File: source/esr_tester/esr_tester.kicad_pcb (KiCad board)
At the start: 2 copper layers, 48.3 x 71.1 mm, 40 parts, among them IC1-1 TL084, J1 Conn_01x01, J2 Conn_01x01

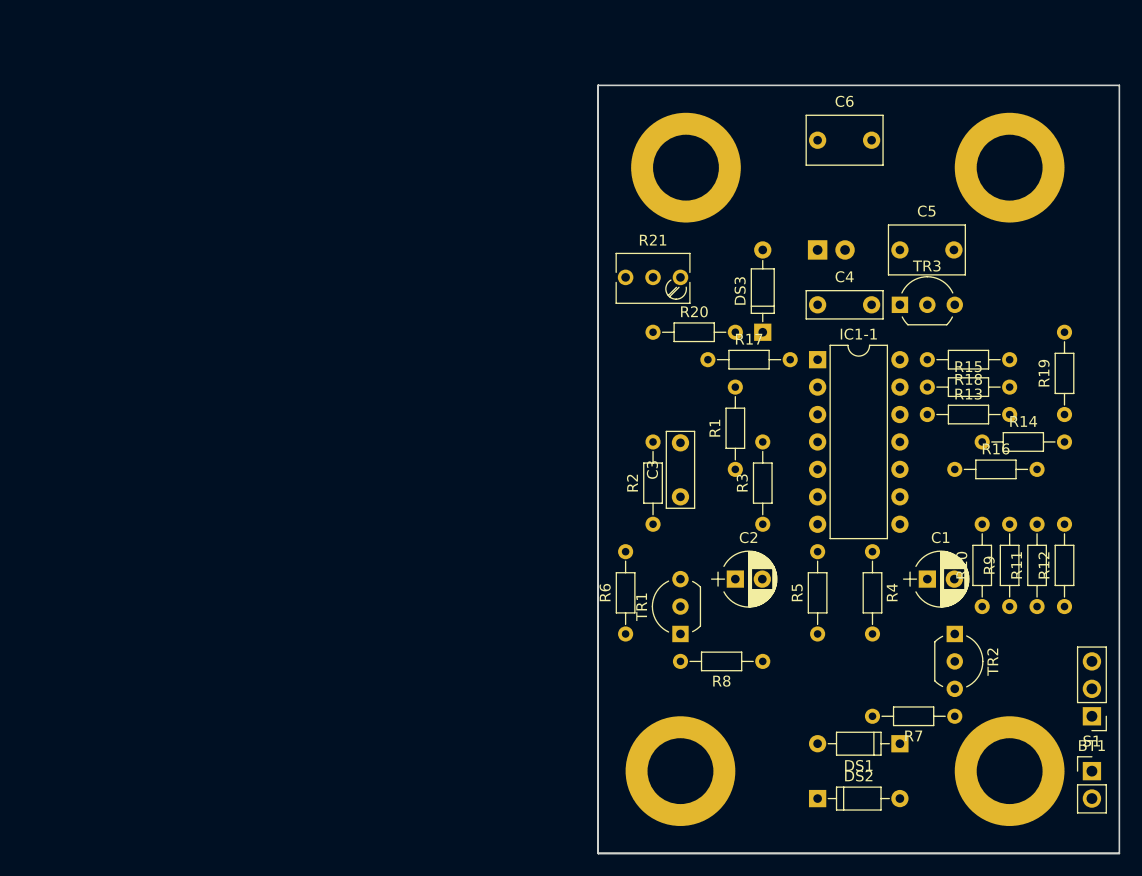
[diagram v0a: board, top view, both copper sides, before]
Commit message: The branch proto2 is for a prototype build with stripboard.
Schematics: changed connector for testing probes (one connector with
two poles instead of two with one each).

CvPcb: Changed some connectors, resistors and diodes footprints.

Pcbnew: A new layout for a stripboard.
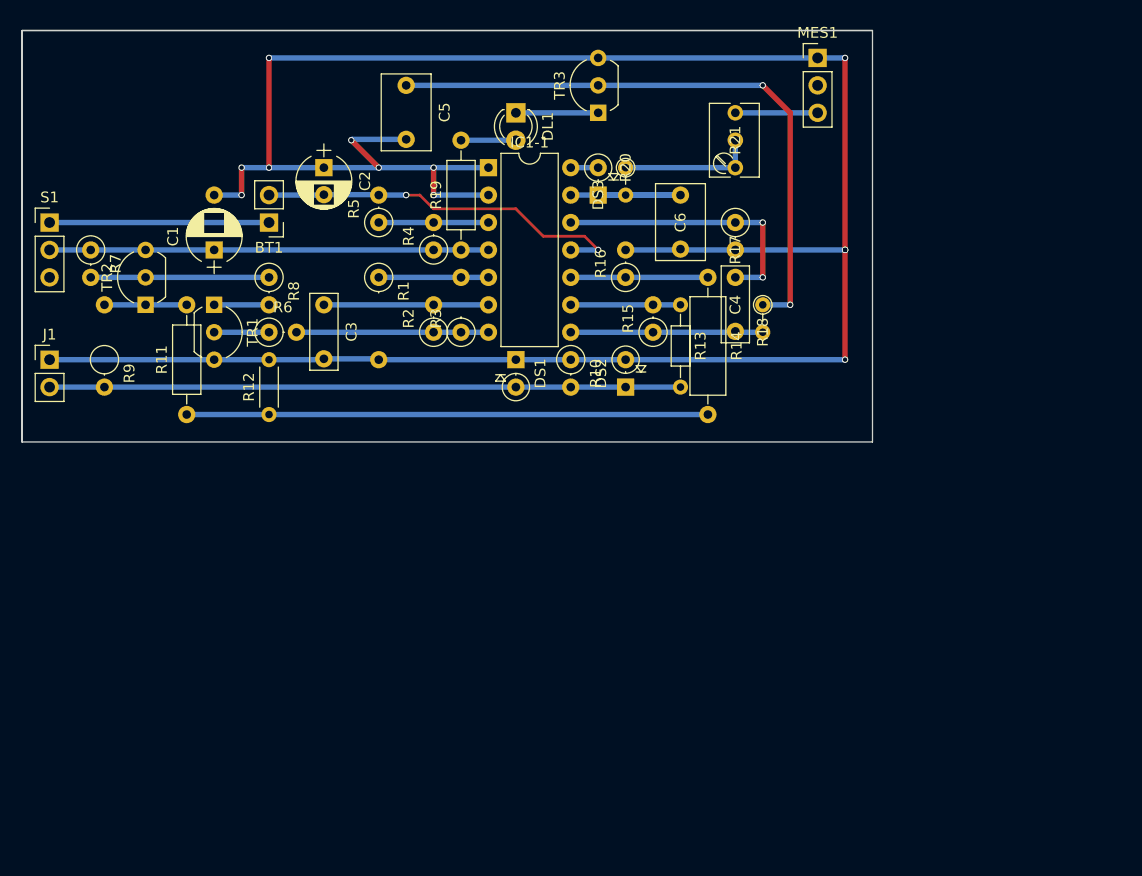
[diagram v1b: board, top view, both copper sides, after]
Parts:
- removed J2: Conn_01x01, Connectors:Banana_Jack_1Pin
- DL1: moved to F.Cu
- DS1, DS2, DS3: footprint Diodes_THT:D_DO-35_SOD27_P7.62mm_Horizontal -> Diodes_THT:D_DO-35_SOD27_P2.54mm_Vertical_KathodeUp
- J1: value Conn_01x01 -> Conn_01x02; footprint Connectors:Banana_Jack_1Pin -> Socket_Strips:Socket_Strip_Straight_1x02_Pitch2.54mm; moved to F.Cu
- MES1: footprint Connectors:Banana_Jack_2Pin -> Socket_Strips:Socket_Strip_Straight_1x03_Pitch2.54mm; moved to F.Cu
- R1, R10, R15, R16, R17, R2, R3, R4, R5, R6, R7, R8, R9: footprint Resistors_THT:R_Axial_DIN0204_L3.6mm_D1.6mm_P7.62mm_Horizontal -> Resistors_THT:R_Axial_DIN0207_L6.3mm_D2.5mm_P2.54mm_Vertical
- R11, R19: footprint Resistors_THT:R_Axial_DIN0204_L3.6mm_D1.6mm_P7.62mm_Horizontal -> Resistors_THT:R_Axial_DIN0207_L6.3mm_D2.5mm_P10.16mm_Horizontal
- R12: footprint Resistors_THT:R_Axial_DIN0204_L3.6mm_D1.6mm_P7.62mm_Horizontal -> Resistors_THT:R_Axial_DIN0204_L3.6mm_D1.6mm_P5.08mm_Horizontal
- R14: footprint Resistors_THT:R_Axial_DIN0204_L3.6mm_D1.6mm_P7.62mm_Horizontal -> Resistors_THT:R_Axial_DIN0309_L9.0mm_D3.2mm_P12.70mm_Horizontal
- R18, R20: footprint Resistors_THT:R_Axial_DIN0204_L3.6mm_D1.6mm_P7.62mm_Horizontal -> Resistors_THT:R_Axial_DIN0204_L3.6mm_D1.6mm_P2.54mm_Vertical
- moved S1 106.8 mm to (55.9, 63.5), turned to 0 degrees
- moved BT1 91.6 mm to (76.2, 63.5), turned to 180 degrees
- moved R7 90.9 mm to (59.7, 66.0), turned to 270 degrees
- moved R9 86.9 mm to (61.0, 76.2), turned to 270 degrees
- moved TR2 80.9 mm to (64.8, 71.1), turned to 90 degrees
- moved R11 80.7 mm to (68.6, 81.3)
- moved R12 75.8 mm to (76.2, 81.3)
- moved C1 72.7 mm to (71.1, 66.0), turned to 90 degrees
- moved J1 69.7 mm to (55.9, 76.2)
- moved R19 57.9 mm to (94.0, 66.0)
- moved R8 57.9 mm to (76.2, 68.6), turned to 270 degrees
- moved R5 55.7 mm to (86.4, 63.5)
- moved C2 53.9 mm to (81.3, 58.4), turned to 270 degrees
- moved TR1 52.9 mm to (71.1, 71.1), turned to 270 degrees
- moved DS1 50.3 mm to (99.1, 76.2), turned to 270 degrees
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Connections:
- BT1 pad 2: (no net) -> /-4.5V
- J1 pad 1: Net-(DS1-Pad2) -> GND
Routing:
- net GND: track 0.00 -> 230.4 mm, vias 0 -> 12
- net Net-(DS1-Pad2): track 0.00 -> 58.4 mm
- net Net-(C5-Pad1): track 0.00 -> 56.9 mm, vias 0 -> 2
- net Net-(R11-Pad1): track 0.00 -> 48.3 mm
- net /+4.5V: track 0.00 -> 45.7 mm
- net /-4.5V: track 0.00 -> 35.3 mm, vias 0 -> 2
- net Net-(C4-Pad1): track 0.00 -> 25.4 mm, vias 0 -> 2
- net Net-(C4-Pad2): track 0.00 -> 20.5 mm
- net Net-(BT1-Pad1): track 0.00 -> 20.3 mm
- net Net-(C6-Pad1): track 0.00 -> 20.3 mm
- net Net-(IC1-1-Pad7): track 0.00 -> 17.8 mm
- net Net-(R7-Pad2): track 0.00 -> 16.5 mm
- net Net-(C3-Pad1): track 0.00 -> 15.2 mm
- net Net-(IC1-1-Pad10): track 0.00 -> 12.7 mm
- net Net-(R20-Pad1): track 0.00 -> 12.7 mm
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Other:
- board size 48.3 x 71.1 mm -> 78.7 x 38.1 mm
- net class Default: trace_width 0.25 -> 0.5
- rule pad_to_mask_clearance: 0.2 -> 0

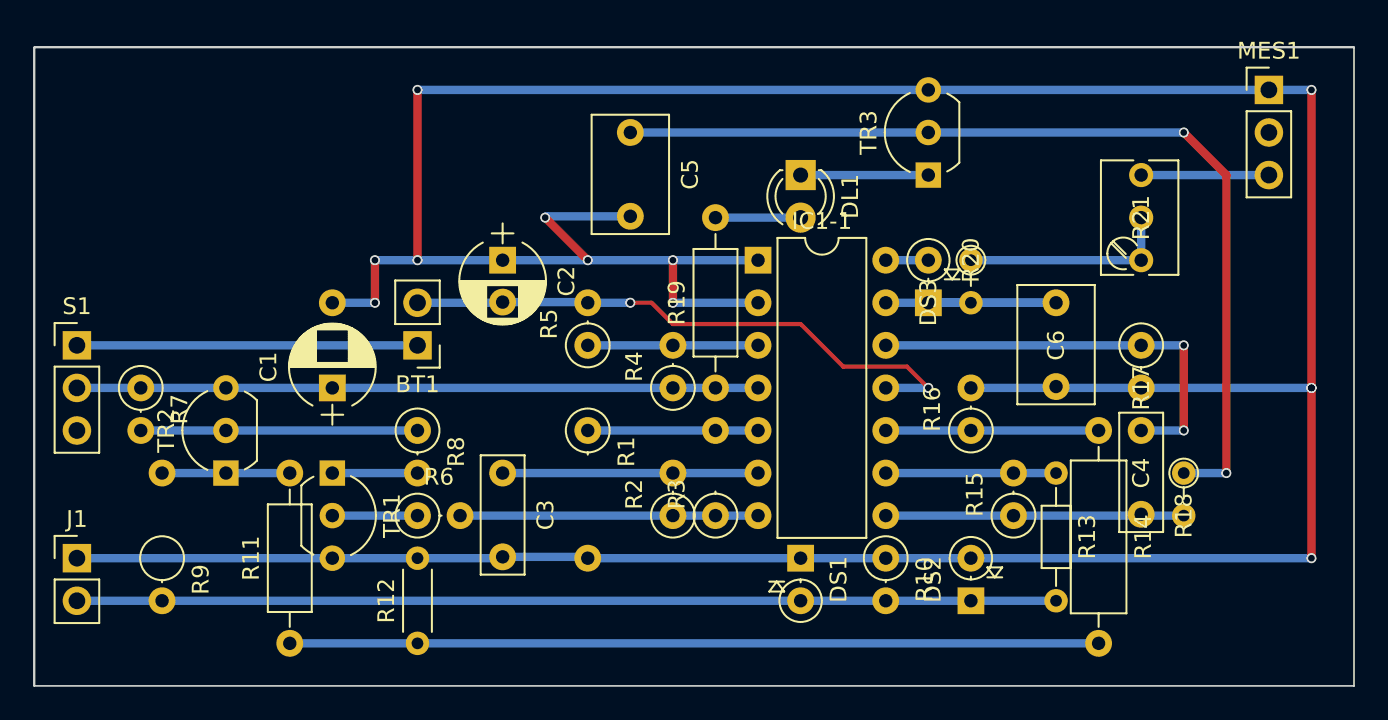
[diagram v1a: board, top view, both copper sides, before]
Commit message: Create a footprint library useful for stripboards.
Modify layout to increase distance between not connected tracks
on Bottom copper layer. This is needed to cleanly cut stripboard tracks.

Plot on a SVG file (for printing). All layesr on one file.
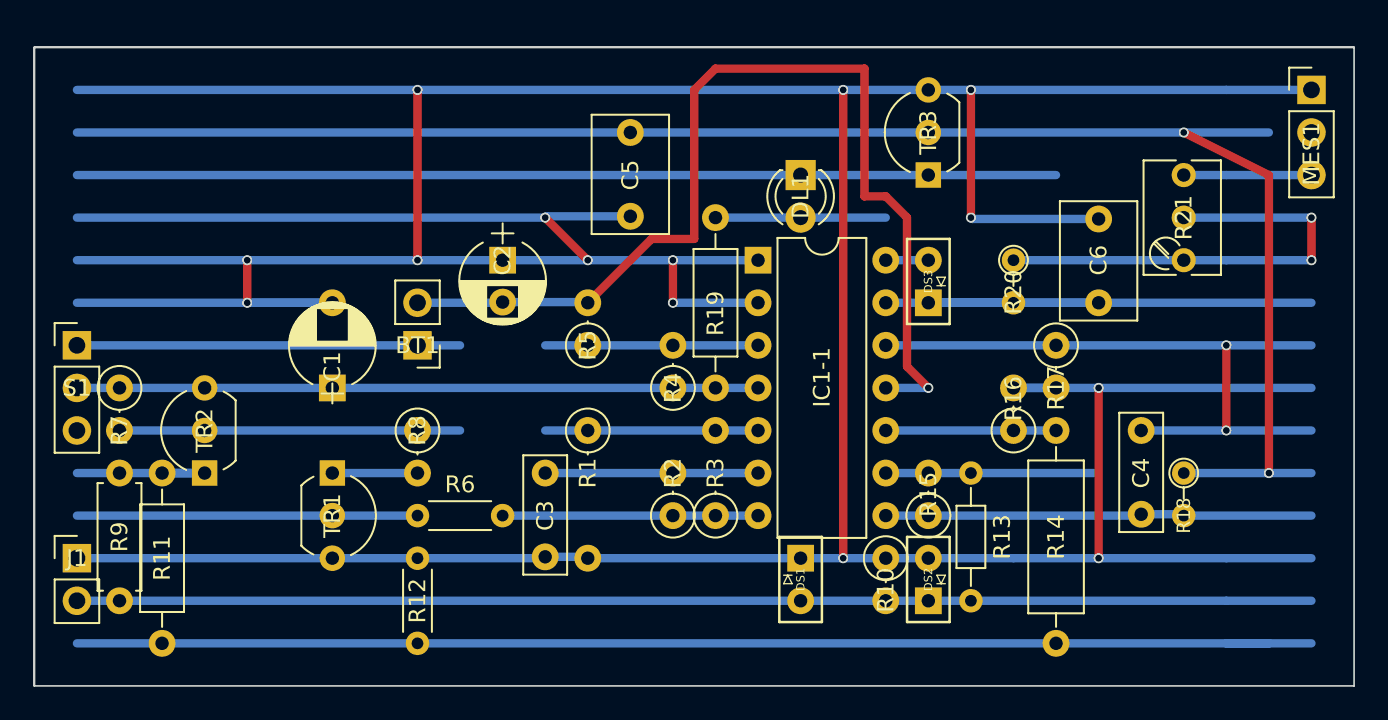
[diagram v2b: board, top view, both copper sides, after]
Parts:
- DS1, DS2, DS3: footprint Diodes_THT:D_DO-35_SOD27_P2.54mm_Vertical_KathodeUp -> stripboard:Diode_2places
- R6: footprint Resistors_THT:R_Axial_DIN0207_L6.3mm_D2.5mm_P2.54mm_Vertical -> Resistors_THT:R_Axial_DIN0204_L3.6mm_D1.6mm_P5.08mm_Horizontal
- R9: footprint Resistors_THT:R_Axial_DIN0207_L6.3mm_D2.5mm_P2.54mm_Vertical -> Resistors_THT:R_Axial_DIN0207_L6.3mm_D2.5mm_P7.62mm_Horizontal
- moved R11 7.62 mm to (61.0, 81.3)
- moved R9 5.68 mm to (58.4, 71.1)
- moved R13 5.08 mm to (109.2, 71.1)
- moved R15 5.08 mm to (106.7, 73.7)
- moved R17 5.08 mm to (114.3, 63.5)
- moved C6 2.54 mm to (116.8, 61.0), turned to 90 degrees
- moved R14 2.54 mm to (114.3, 68.6)
- moved R16 2.54 mm to (111.8, 68.6)
- moved R20 2.54 mm to (111.8, 58.4)
- moved R21 2.54 mm to (121.9, 58.4)
- moved C3 2.54 mm to (83.8, 71.1)
- moved DS2 2.54 mm to (106.7, 78.7)
- moved MES1 2.54 mm to (129.5, 48.3)
- moved C1 1.27 mm to (71.1, 64.8)
- moved R7 1.27 mm to (58.4, 66.0)
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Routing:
- net GND: track 230.4 -> 339.8 mm, vias 12 -> 14
- net Net-(DL1-Pad1): track 7.62 -> 58.4 mm
- net Net-(C5-Pad1): track 56.9 -> 102.2 mm
- net Net-(R11-Pad1): track 48.3 -> 78.7 mm
- net /-4.5V: track 35.3 -> 61.7 mm, vias 2 -> 1
- net Net-(C6-Pad1): track 20.3 -> 40.6 mm
- net Net-(R6-Pad1): track 5.08 -> 20.3 mm
- net Net-(DS1-Pad2): track 58.4 -> 73.7 mm
- net Net-(R20-Pad1): track 12.7 -> 27.9 mm, vias 0 -> 2
- net Net-(C4-Pad1): track 25.4 -> 40.6 mm
- net Net-(R11-Pad2): track 7.62 -> 12.7 mm
- net Net-(DL1-Pad2): track 5.08 -> 10.2 mm
- net Net-(C4-Pad2): track 20.5 -> 25.5 mm
- net Net-(R7-Pad2): track 16.5 -> 20.3 mm
- net Net-(IC1-1-Pad9): track 10.2 -> 12.7 mm
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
